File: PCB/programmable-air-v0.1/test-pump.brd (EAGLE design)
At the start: 28.1 x 28.1 mm, 1 part

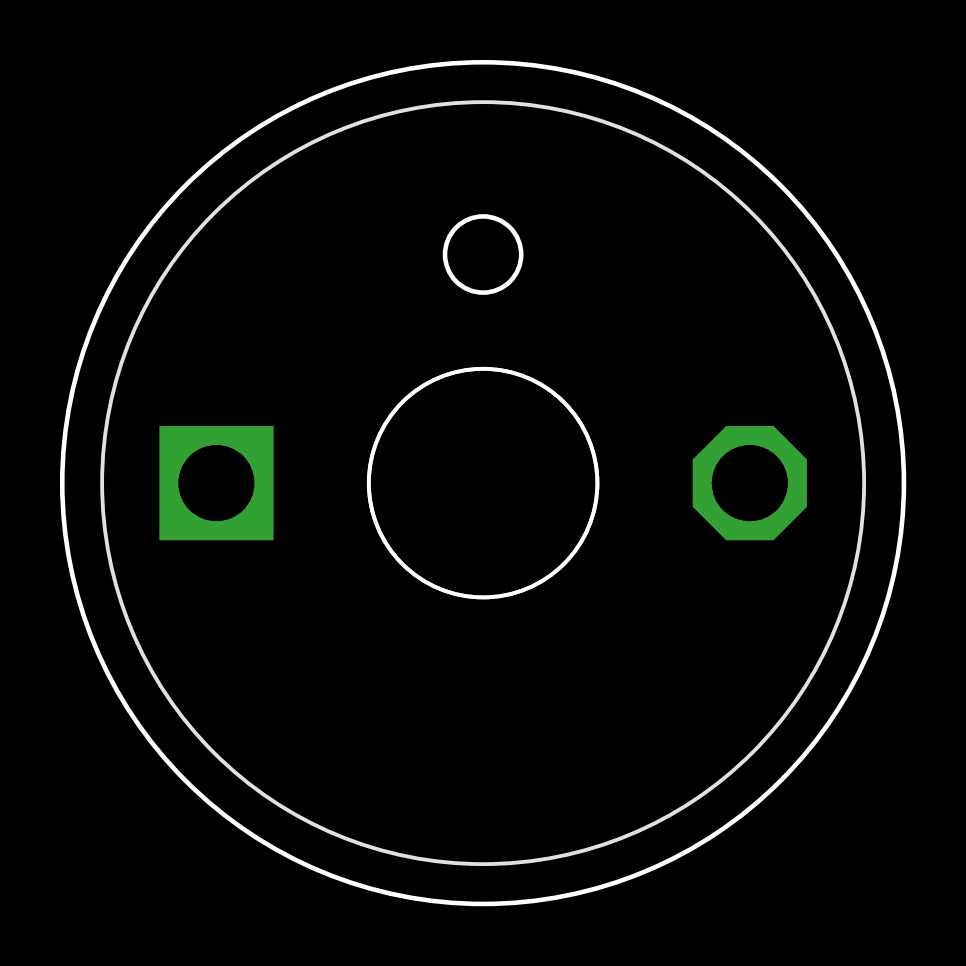
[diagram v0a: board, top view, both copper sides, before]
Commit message: Made pump nad valve PCB library. PCB Mockup made. Added arduino nano footprint.
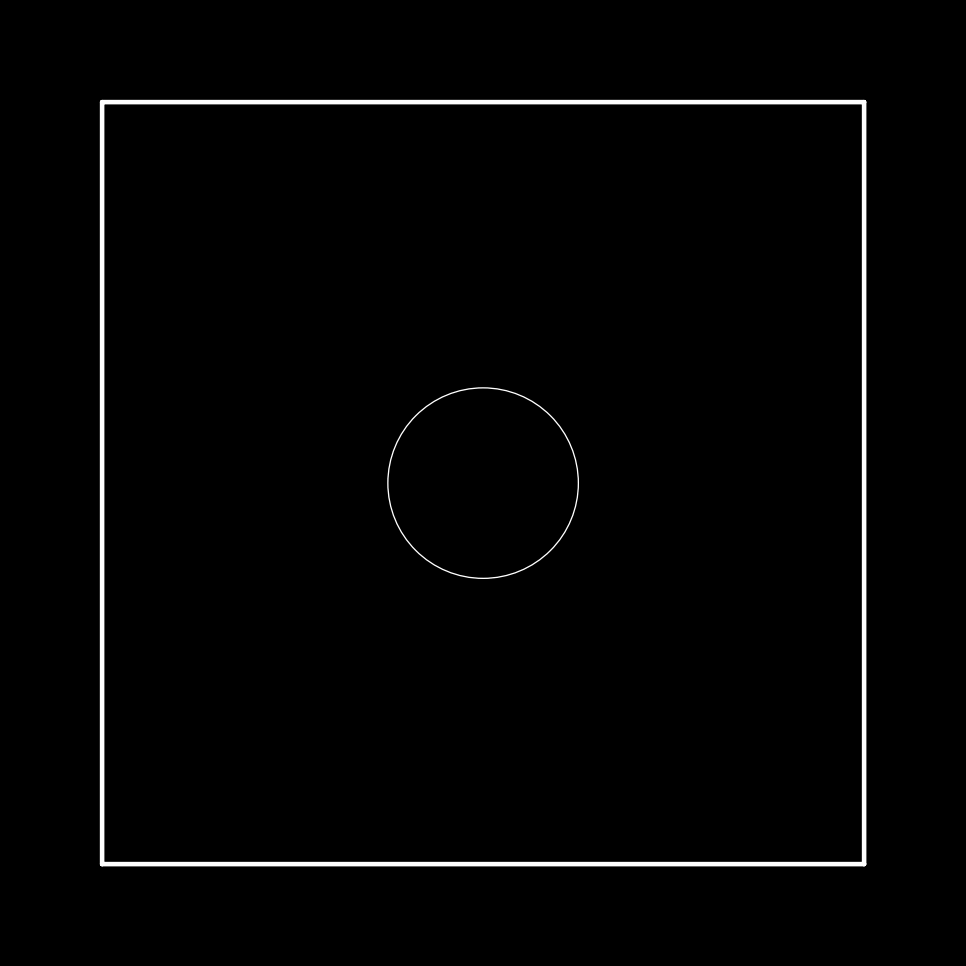
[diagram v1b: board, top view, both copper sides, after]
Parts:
- removed E$1: (no value), programmable-air-components:A5F083
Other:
- board size 28.1 x 28.1 mm -> 25.4 x 25.4 mm
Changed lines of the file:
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@@
 <settings>
 <setting alwaysvectorfont="no"/>
-<setting keepoldvectorfont="yes"/>
 <setting verticaltext="up"/>
 </settings>
@@
 <layers>
 <layer number="1" name="Top" color="4" fill="1" visible="yes" active="yes"/>
-<layer number="2" name="Route2" color="1" fill="3" visible="no" active="no"/>
-<layer number="3" name="Route3" color="4" fill="3" visible="no" active="no"/>
-<layer number="4" name="Route4" color="1" fill="4" visible="no" active="no"/>
-<layer number="5" name="Route5" color="4" fill="4" visible="no" active="no"/>
-<layer number="6" name="Route6" color="1" fill="8" visible="no" active="no"/>
-<layer number="7" name="Route7" color="4" fill="8" visible="no" active="no"/>
-<layer number="8" name="Route8" color="1" fill="2" visible="no" active="no"/>
-<layer number="9" name="Route9" color="4" fill="2" visible="no" active="no"/>
-<layer number="10" name="Route10" color="1" fill="7" visible="no" active="no"/>
-<layer number="11" name="Route11" color="4" fill="7" visible="no" active="no"/>
-<layer number="12" name="Route12" color="1" fill="5" visible="no" active="no"/>
-<layer number="13" name="Route13" color="4" fill="5" visible="no" active="no"/>
-<layer number="14" name="Route14" color="1" fill="6" visible="no" active="no"/>
-<layer number="15" name="Route15" color="4" fill="6" visible="no" active="no"/>
 <layer number="16" name="Bottom" color="1" fill="1" visible="yes" active="yes"/>
 <layer number="17" name="Pads" color="2" fill="1" visible="yes" active="yes"/>
 <layer number="18" name="Vias" color="2" fill="1" visible="yes" active="yes"/>
 <layer number="19" name="Unrouted" color="6" fill="1" visible="yes" active="yes"/>
-<layer number="20" name="Dimension" color="15" fill="1" visible="yes" active="yes"/>
+<layer number="20" name="Dimension" color="24" fill="1" visible="yes" active="yes"/>
 <layer number="21" name="tPlace" color="7" fill="1" visible="yes" active="yes"/>
 <layer number="22" name="bPlace" color="7" fill="1" visible="yes" active="yes"/>
@@
 <layer number="44" name="Drills" color="7" fill="1" visible="no" active="yes"/>
 <layer number="45" name="Holes" color="7" fill="1" visible="yes" active="yes"/>
-<layer number="46" name="Milling" color="3" fill="1" visible="no" active="yes"/>
+<layer number="46" name="Milling" color="3" fill="1" visible="yes" active="yes"/>
 <layer number="47" name="Measures" color="7" fill="1" visible="no" active="yes"/>
 <layer number="48" name="Document" color="7" fill="1" visible="yes" active="yes"/>
@@
 <layer number="51" name="tDocu" color="7" fill="1" visible="yes" active="yes"/>
 <layer number="52" name="bDocu" color="7" fill="1" visible="yes" active="yes"/>
-<layer number="90" name="Modules" color="5" fill="1" visible="no" active="no"/>
-<layer number="91" name="Nets" color="2" fill="1" visible="no" active="no"/>
-<layer number="92" name="Busses" color="1" fill="1" visible="no" active="no"/>
-<layer number="93" name="Pins" color="2" fill="1" visible="no" active="no"/>
-<layer number="94" name="Symbols" color="4" fill="1" visible="no" active="no"/>
-<layer number="95" name="Names" color="7" fill="1" visible="no" active="no"/>
-<layer number="96" name="Values" color="7" fill="1" visible="no" active="no"/>
-<layer number="97" name="Info" color="7" fill="1" visible="no" active="no"/>
-<layer number="98" name="Guide" color="6" fill="1" visible="no" active="no"/>
 </layers>
 <board>
 <plain>
-<circle x="0" y="0" radius="14.02760625" width="0.1524" layer="20"/>
-<hole x="0" y="0" drill="7.62"/>
-<circle x="0" y="7.62" radius="1.27" width="0.1524" layer="20"/>
+<polygon width="0.1524" layer="20">
+<vertex x="-12.7" y="12.7"/>
+<vertex x="12.7" y="12.7"/>
+<vertex x="12.7" y="-12.7"/>
+<vertex x="-12.7" y="-12.7"/>
+</polygon>
+<hole x="0" y="0" drill="6.35"/>
 </plain>
 <attributes>
@@
 </autorouter>
 <elements>
-<element name="E$1" library="programmable-air-components" package="A5F083" value="" x="0" y="0"/>
 </elements>
 <signals>
